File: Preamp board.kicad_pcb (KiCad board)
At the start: 2 copper layers, 19.1 x 59.6 mm, 23 parts, among them J1 Coil, J2 Rx, J3 DC, J4 DC, U1 Preamp

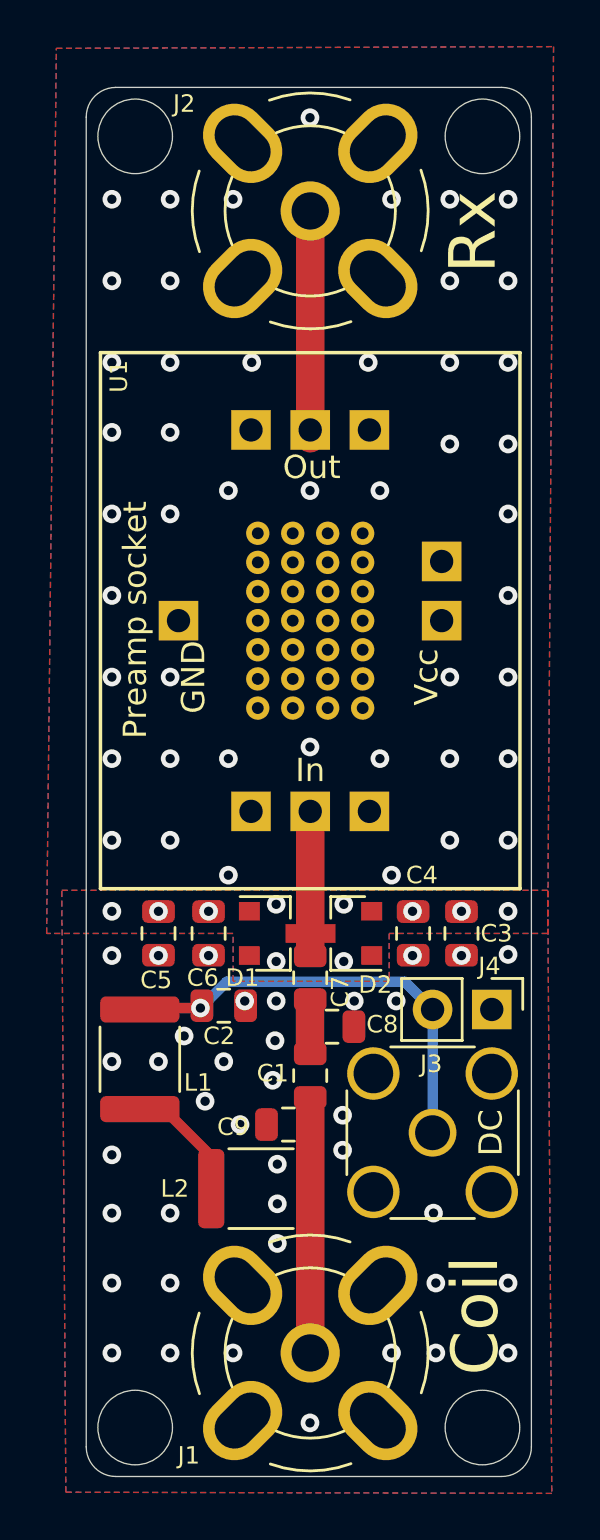
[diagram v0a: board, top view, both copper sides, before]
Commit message: Changed: updated preamp footprint. Made 3D settings
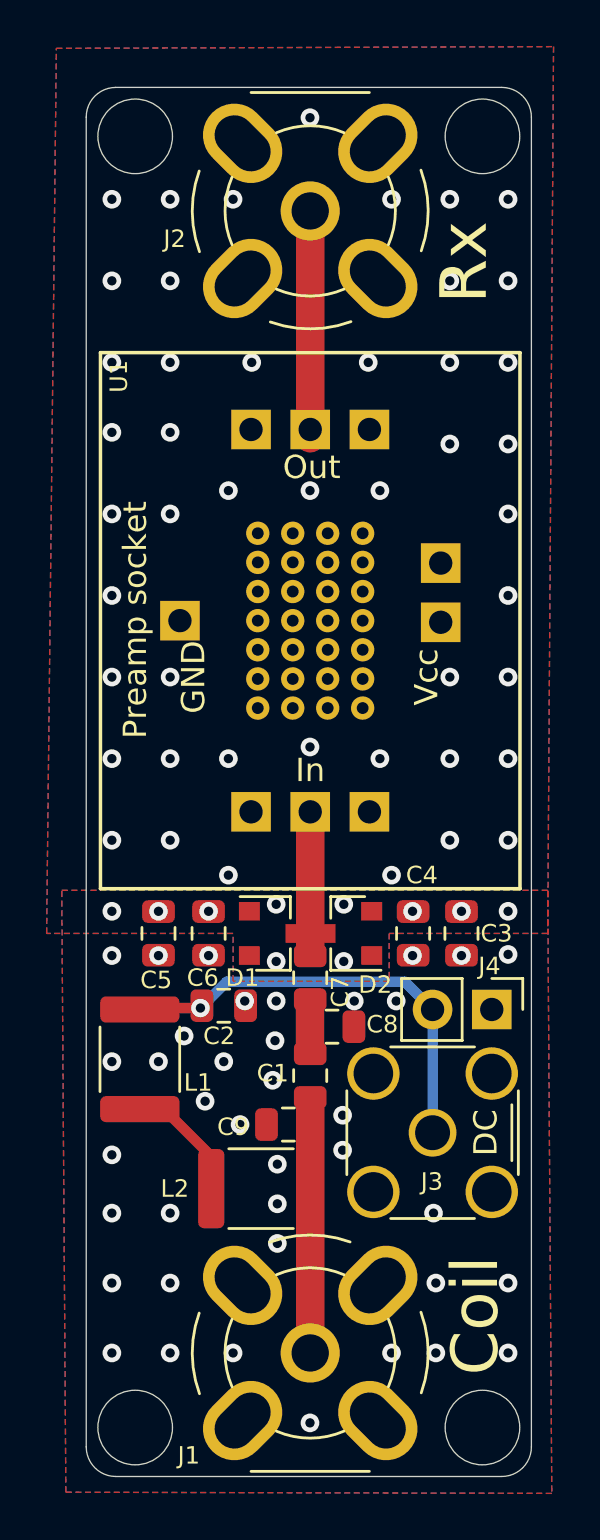
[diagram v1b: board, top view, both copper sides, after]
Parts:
- J3: footprint Connector_Coaxial:SMA_Amphenol_132134-16_Vertical -> _Custom:SMA_Amphenol_132134-16_Vertical
- turned J2 to 180 degrees
- turned J3 to 90 degrees
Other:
- board text added: "03/2020 v0.2"
- board text removed: "02/2020 v0.1"
- board text removed: "preamp afstand philips aanhouden RF ground scheiden met C's"

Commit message: Changed: header hole size, header to preci-dip header
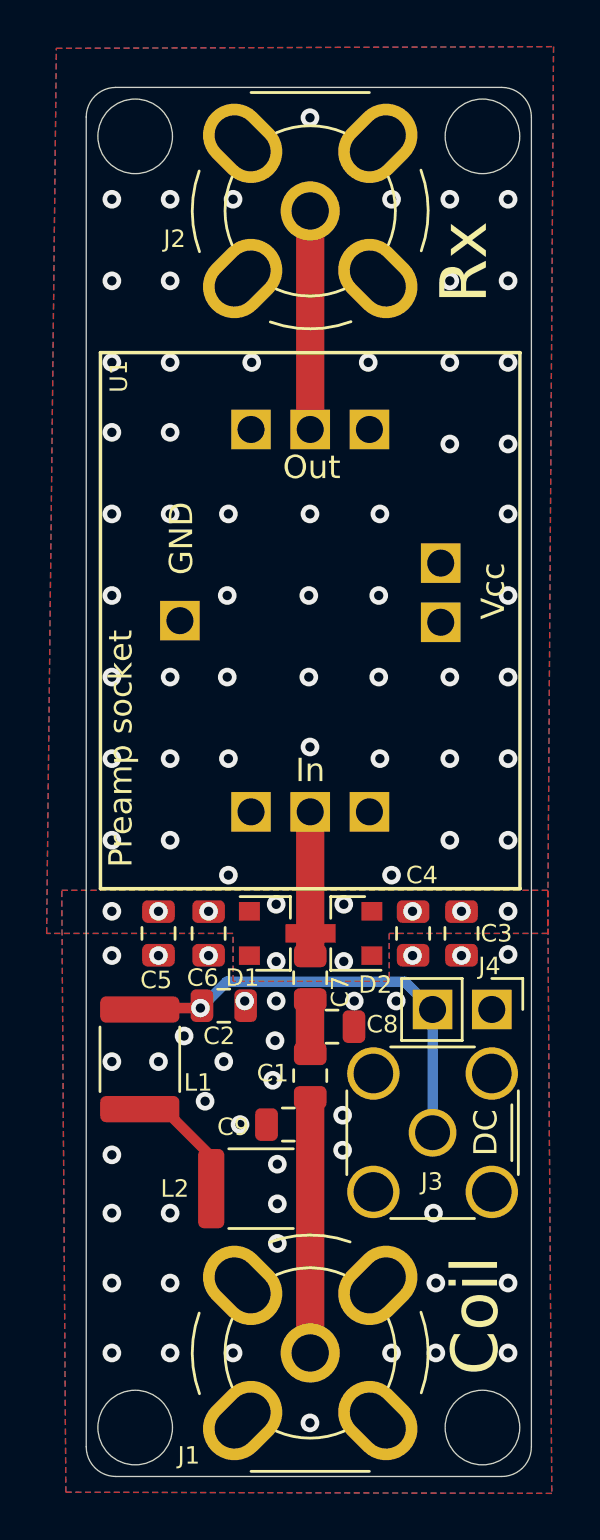
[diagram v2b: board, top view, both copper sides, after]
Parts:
- J4: footprint Connector_PinHeader_2.54mm:PinHeader_1x02_P2.54mm_Vertical -> _Custom:Preci-dip_PinHeader_1x02_rect
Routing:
- net GNDA: vias 56 -> 62

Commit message: Small changes
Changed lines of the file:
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@@
-(kicad_pcb (version 20171130) (host pcbnew "(5.1.5)-3")
+(kicad_pcb (version 20171130) (host pcbnew 5.1.5)
   (general
     (thickness 1.6)
@@
     (45 Margin user)
     (46 B.CrtYd user hide)
-    (47 F.CrtYd user hide)
+    (47 F.CrtYd user)
     (48 B.Fab user hide)
     (49 F.Fab user hide)
@@
     (aux_axis_origin 0 0)
     (grid_origin 72.45 118.5)
-    (visible_elements 7FFFFF7F)
+    (visible_elements 7FFBFF7F)
     (pcbplotparams
       (layerselection 0x010fc_ffffffff)
@@
       (effects (font (size 0.75 0.75) (thickness 0.15)))
     )
-    (pad 1 thru_hole rect (at 0 0 270) (size 1.7 1.7) (drill 1.16) (layers *.Cu *.Mask)
+    (pad 1 thru_hole rect (at 0 0 270) (size 1.7 1.7) (drill 1.4) (layers *.Cu *.Mask)
       (net 4 GNDS))
-    (pad 2 thru_hole rect (at 0 2.54 270) (size 1.7 1.7) (drill 1.16) (layers *.Cu *.Mask)
+    (pad 2 thru_hole rect (at 0 2.54 270) (size 1.7 1.7) (drill 1.4) (layers *.Cu *.Mask)
       (net 8 "Net-(C2-Pad2)"))
     (model :_Custom_3D:preci-dip_solder-tail_2pin_pcb_connector_310-87-102-41-001101.stp
@@
   (segment (start 65 128.20001) (end 67.79998 128.20001) (width 0.45) (layer F.Cu) (net 8))
   (segment (start 72.51 120.29) (end 72.51 119.38) (width 0.25) (layer F.Cu) (net 9))
-  (segment (start 71.9 125) (end 72.51 125) (width 0.25) (layer F.Cu) (net 9))
-  (segment (start 73.15 125) (end 72.51 125) (width 0.25) (layer F.Cu) (net 9))
   (segment (start 72.51 119.7828) (end 72.51 125.8) (width 1.21645) (layer F.Cu) (net 9))
+  (segment (start 73.15 125) (end 72.51 125) (width 0.25) (layer F.Cu) (net 9) (status 1000000))
+  (segment (start 71.9 125) (end 72.51 125) (width 0.25) (layer F.Cu) (net 9) (status 1000000))
   (zone (net 3) (net_name GNDA) (layer F.Cu) (hatch edge 0.508)
     (priority 1)

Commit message: Small changes. V0.2
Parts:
- moved D1 0.12 mm to (71.0, 125.0)
- moved D2 0.10 mm to (74.0, 125.0)
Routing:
- net Net-(C7-Pad2): track 8.18 -> 6.84 mm
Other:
- rule pad_to_mask_clearance: 0.051 -> 0
- board text added: "04/2020 v0.3"
- board text removed: "03/2020 v0.2"
